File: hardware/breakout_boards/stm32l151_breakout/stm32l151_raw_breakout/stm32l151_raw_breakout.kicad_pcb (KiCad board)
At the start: 2 copper layers, 20.8 x 61 mm, 50 parts, among them U1 STM32L151CCTx

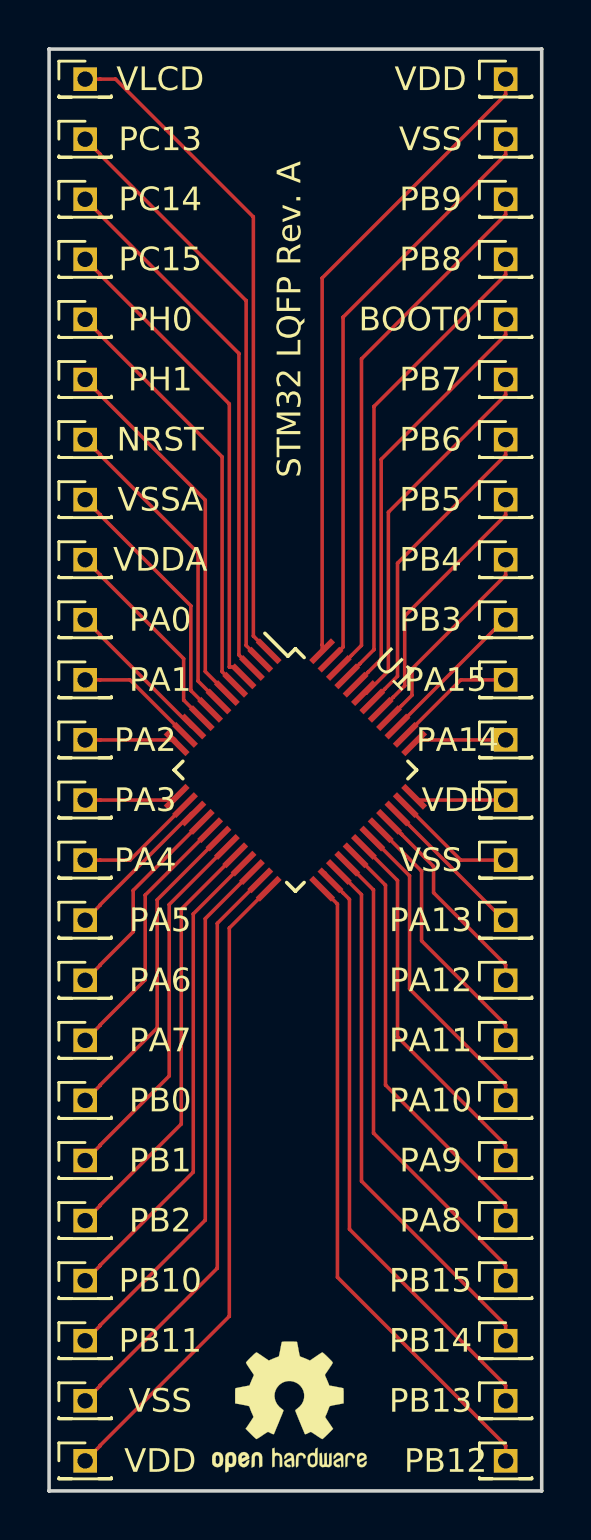
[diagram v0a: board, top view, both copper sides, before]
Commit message: Extract out UI class
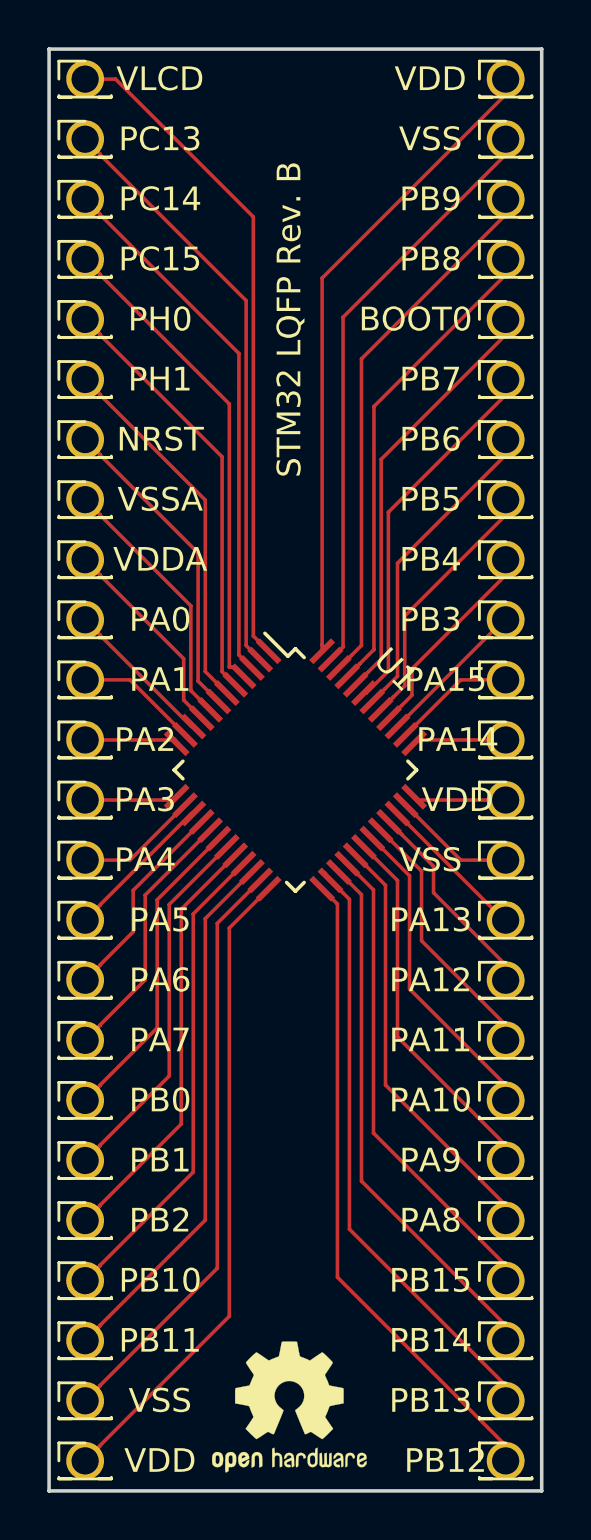
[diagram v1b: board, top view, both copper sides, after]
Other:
- board text added: "STM32 LQFP Rev. B"
- board text removed: "STM32 LQFP Rev. A"
